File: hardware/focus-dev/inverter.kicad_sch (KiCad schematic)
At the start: 57 parts, among them J5 Conn_01x01, J6 Conn_01x01, J7 Conn_01x01, Q1 IPD90N04S4L04, Q2 IPD90N04S4L04, Q3 IPD90N04S4L04, Q4 IPD90N04S4L04, Q5 IPD90N04S4L04, Q6 IPD90N04S4L04, U3 INA181A3, U4 LM2105D, U5 INA181A3, U6 LM2105D, U7 INA181A3, U8 LM2105D

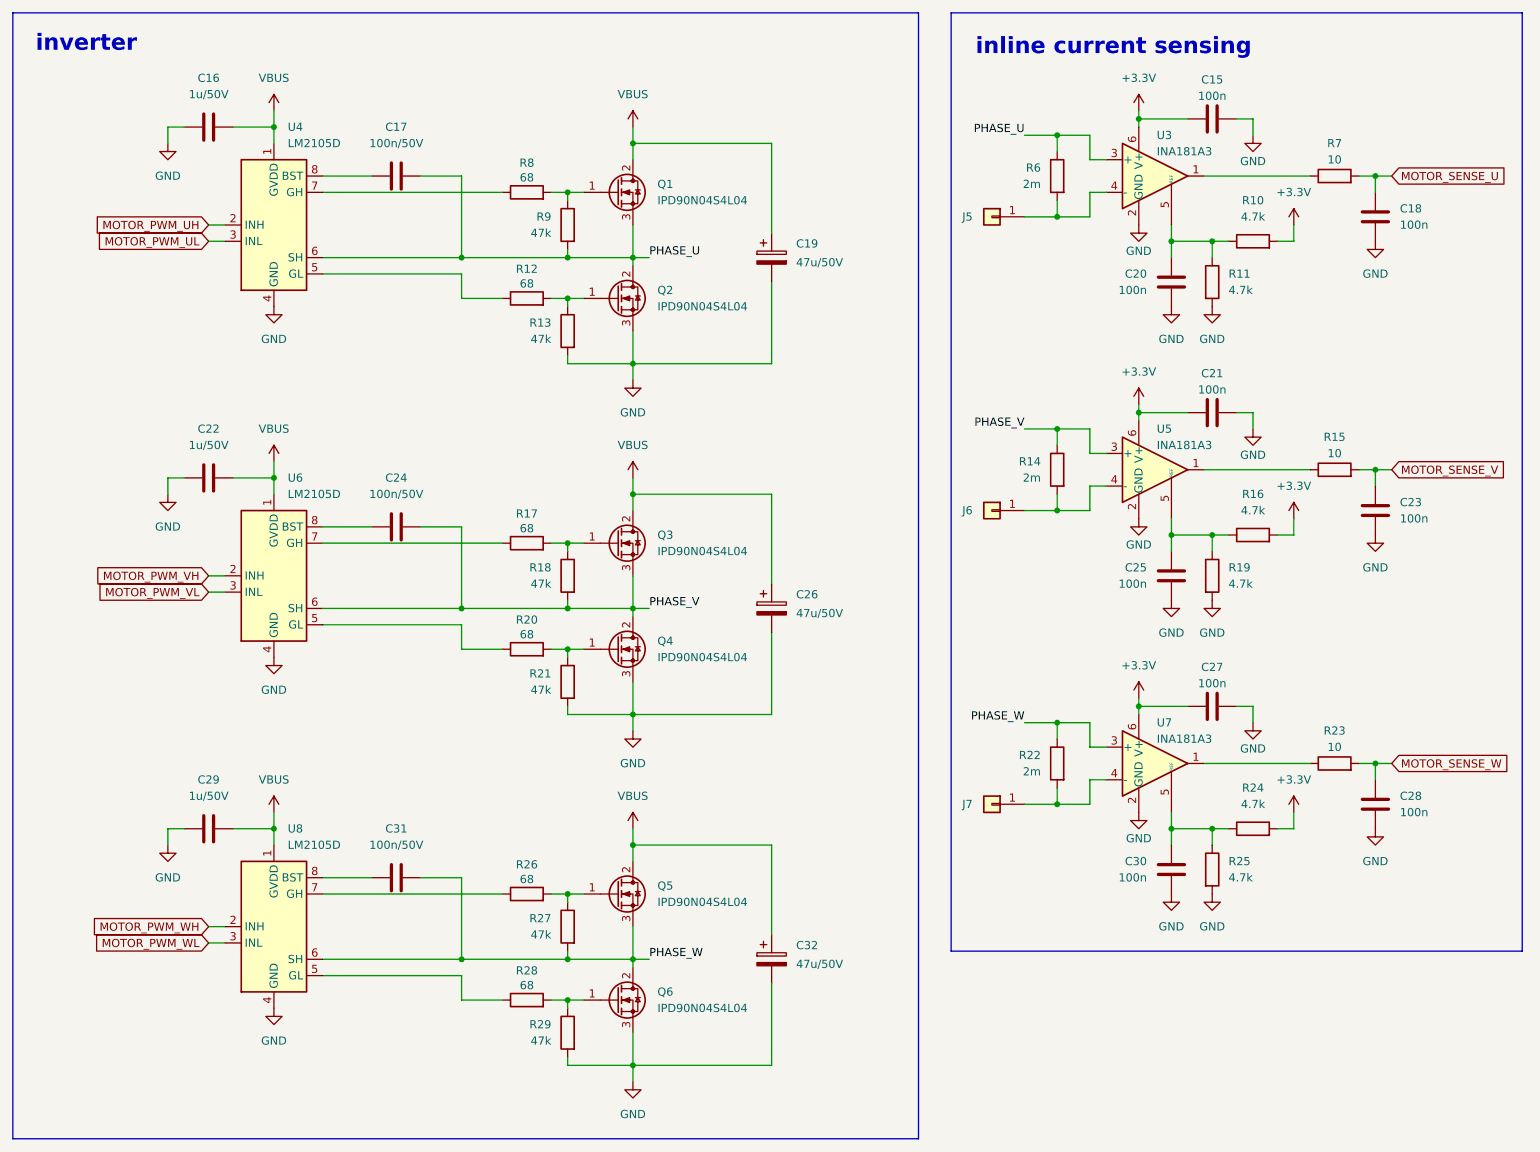
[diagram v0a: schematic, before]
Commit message: wip: remove onboard encoders
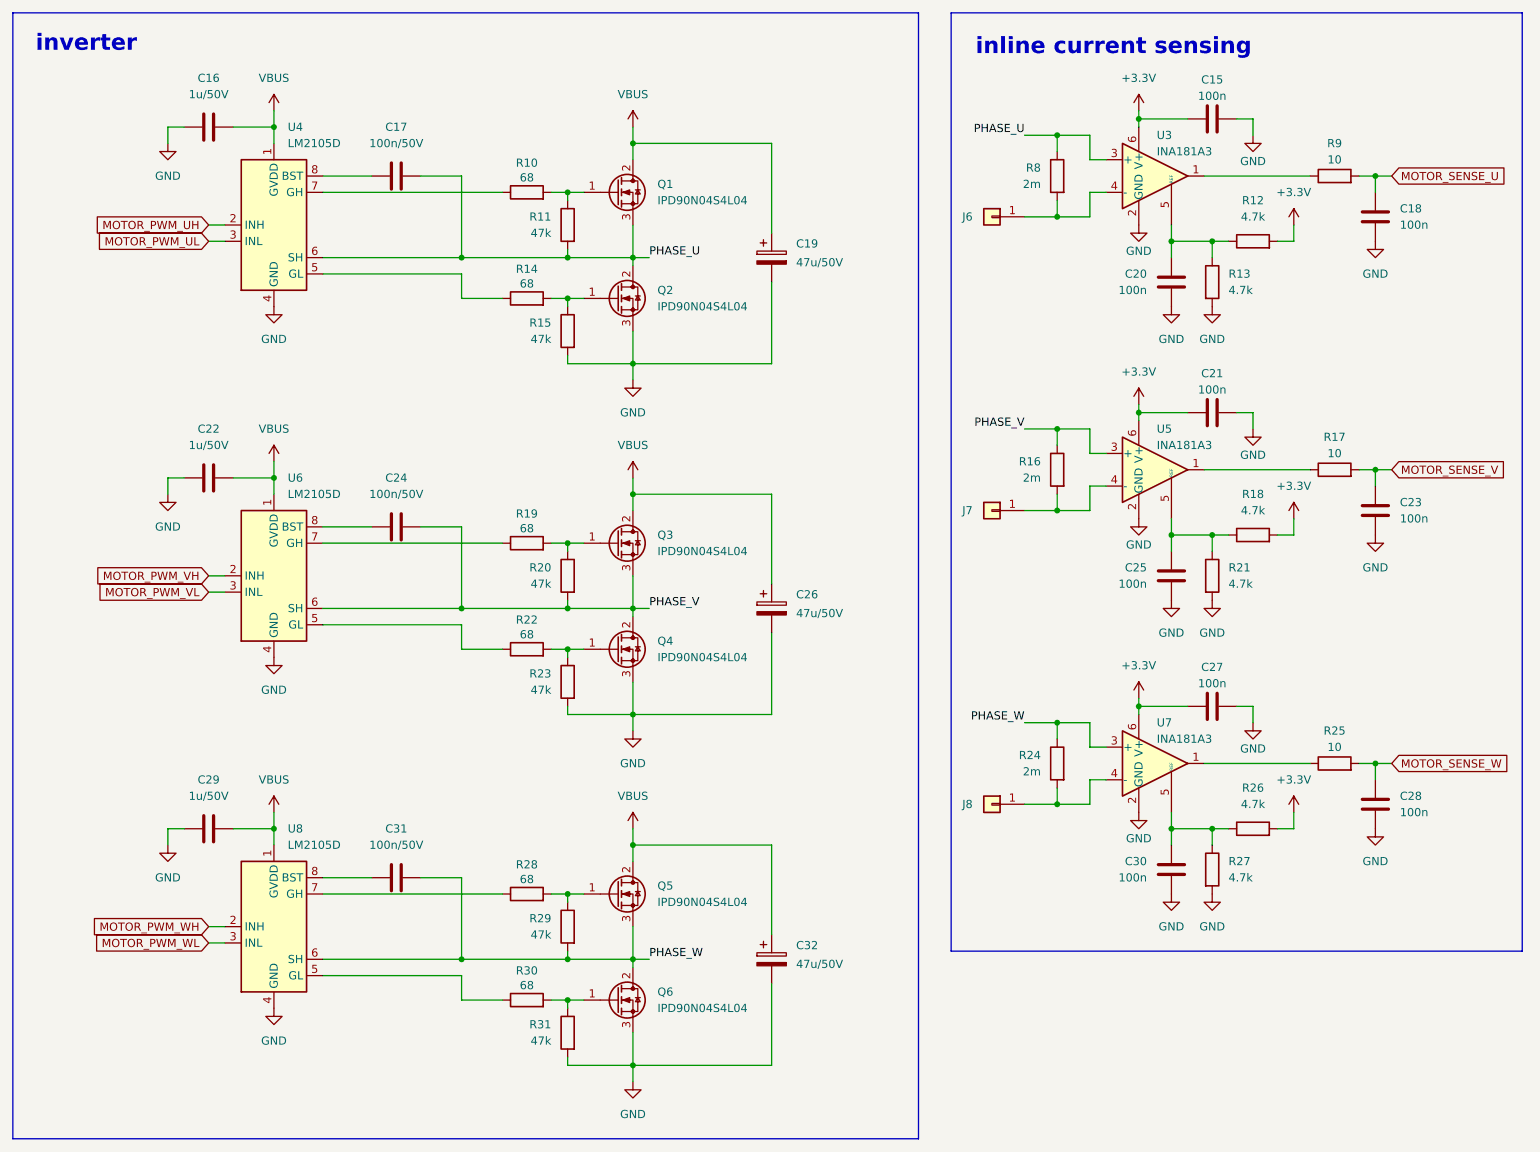
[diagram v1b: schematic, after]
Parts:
- renumbered J5 to J6, J6 to J7, J7 to J8, R8 to R10, R9 to R11, R10 to R12, R11 to R13, R12 to R14, R13 to R15, R14 to R16, R15 to R17, R16 to R18, R17 to R19, R18 to R20, R19 to R21, R20 to R22, R21 to R23, R22 to R24, R23 to R25, R24 to R26, R25 to R27, R26 to R28, R27 to R29, R28 to R30, R29 to R31, R6 to R8, R7 to R9
